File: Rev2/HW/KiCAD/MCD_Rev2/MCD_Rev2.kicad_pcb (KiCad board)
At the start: 2 copper layers, 196.3 x 114.7 mm, 77 parts, among them J1 DBUS_LOW, J2 DBUS_HIGH, J3 ABUS, J4 POWER, J6 Conn_01x02_Male, SW1 SW_Push, U1 XC9572XL-PC44, U10 STM1001LWX6F, U2 AS6C1008-55PCN, U3 AS6C1008-55PCN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

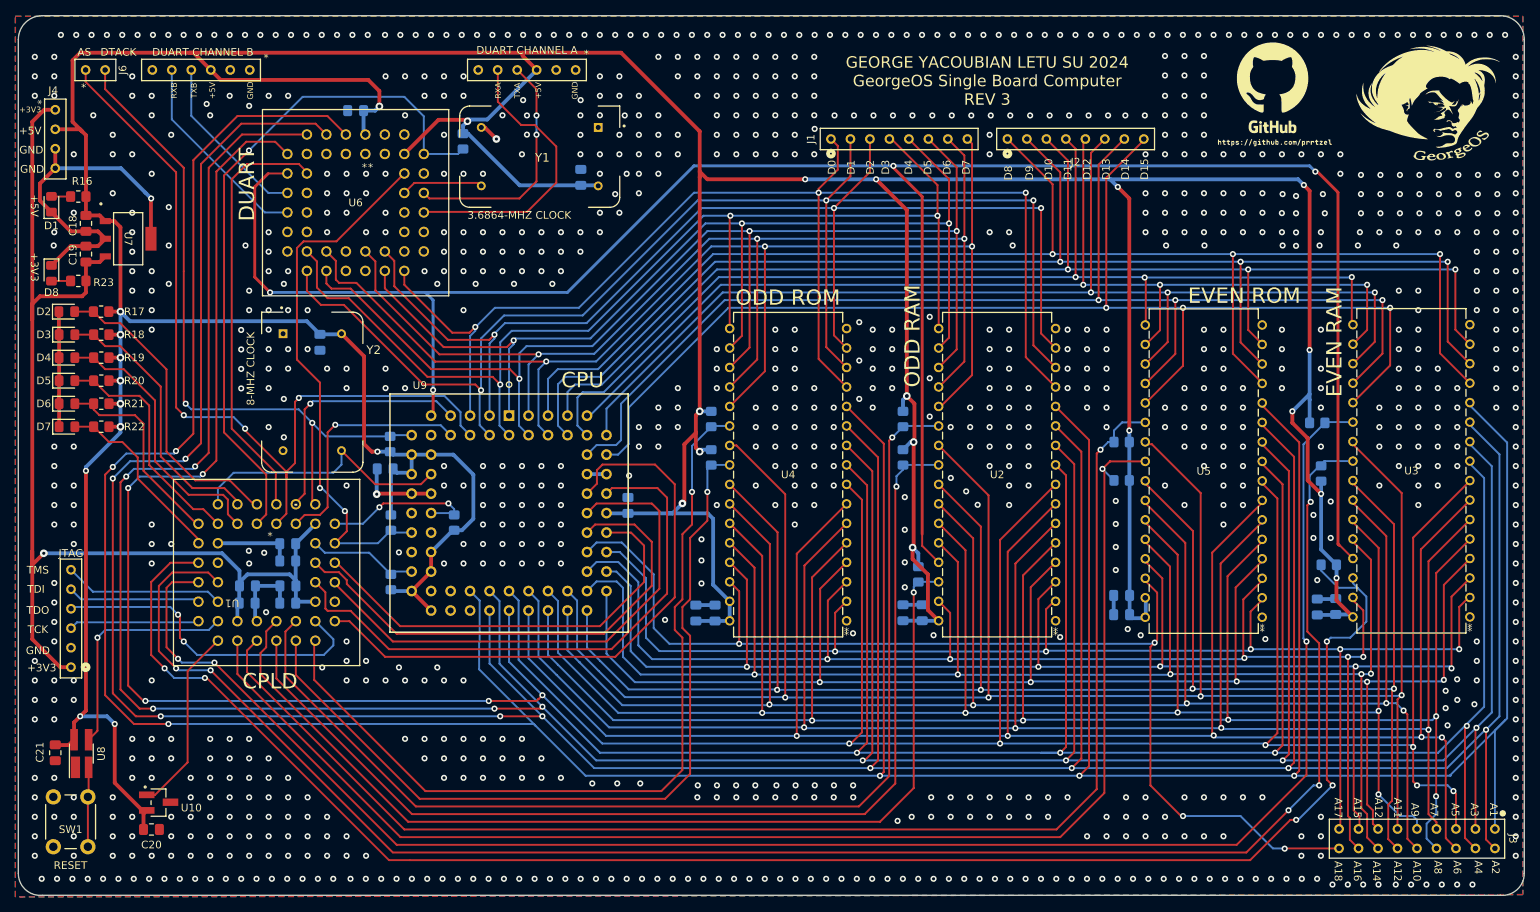
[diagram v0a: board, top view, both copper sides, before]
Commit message: load_srec implemented
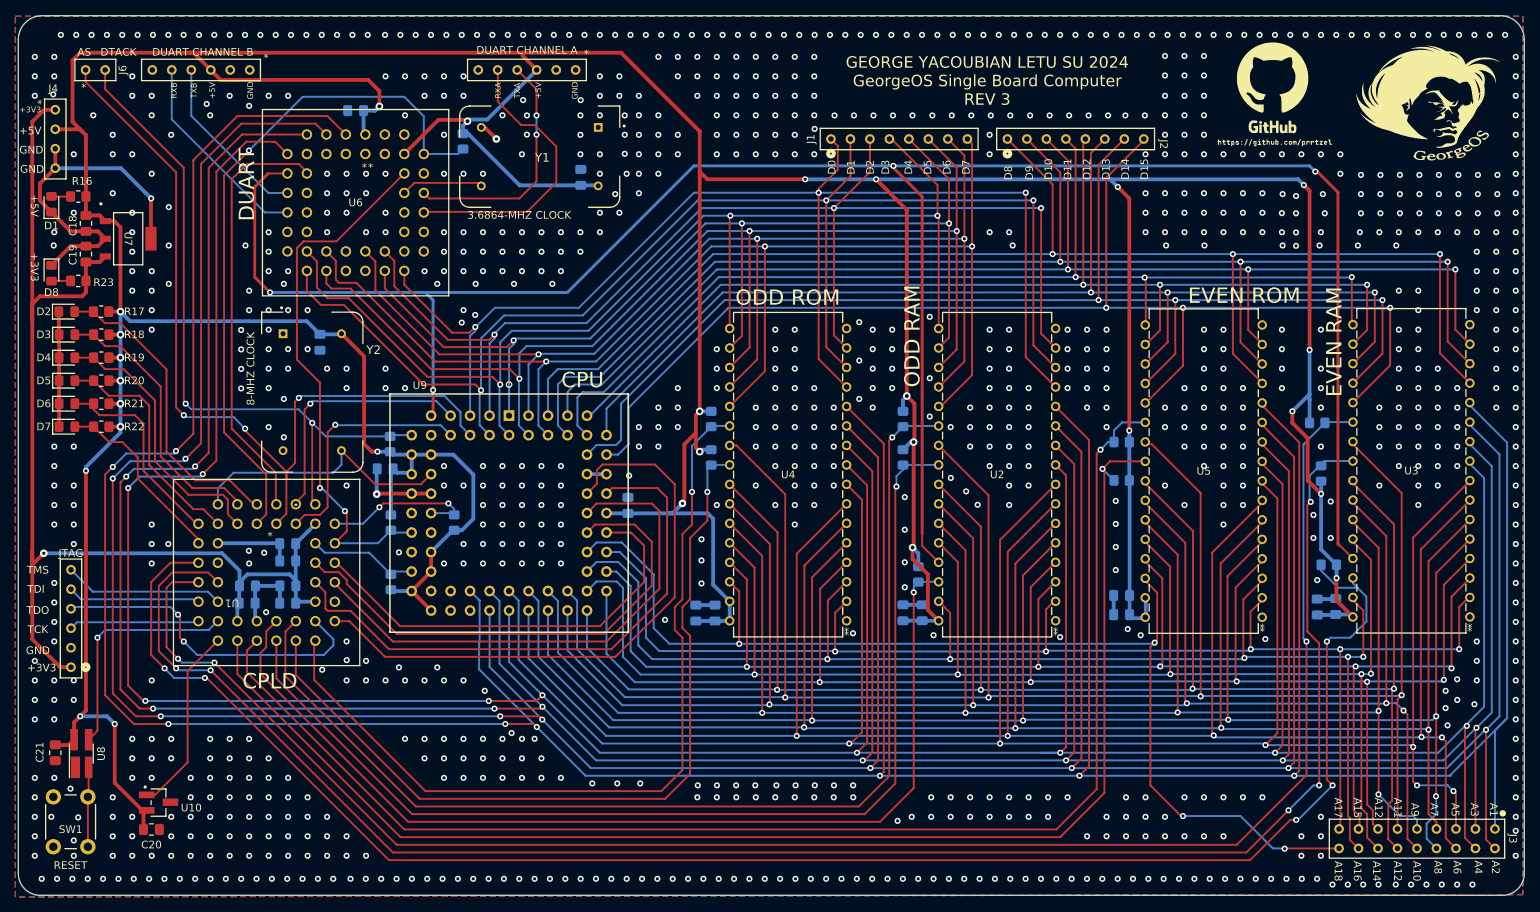
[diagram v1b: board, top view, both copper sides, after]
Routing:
- net A1: track 521.9 -> 522.5 mm, vias 6 -> 8
- net GND: vias 1033 -> 1038

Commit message: finished pcb
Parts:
- J7: renamed from DUART CHANNEL A
- J8: renamed from DUART CHANNEL B
- renumbered JTAG to J5
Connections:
- U6 pad 3: unconnected-(U6-Pad3) -> GND
- U6 pad 40: unconnected-(U6-Pad40) -> GND
- U6 pad 42: unconnected-(U6-Pad42) -> GND
- U6 pad 43: unconnected-(U6-Pad43) -> GND
- U6 pad 5: unconnected-(U6-Pad5) -> GND
- U6 pad 8: unconnected-(U6-Pad8) -> GND

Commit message: finished pcb
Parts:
- added R24: 4k7, Resistor_SMD:R_0805_2012Metric_Pad1.20x1.40mm_HandSolder, B.Cu at (142.2, 95.2)
- added R25: 4k7, Resistor_SMD:R_0805_2012Metric_Pad1.20x1.40mm_HandSolder, B.Cu at (142.2, 92.5)
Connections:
- U6 pad 5: GND -> Net-(U6-Pad5)
- U6 pad 8: GND -> Net-(U6-Pad8)
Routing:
- net Net-(U6-Pad8): track 0.00 -> 7.09 mm
- net Net-(U6-Pad5): track 0.00 -> 3.14 mm
- net GND: vias 1038 -> 1035
